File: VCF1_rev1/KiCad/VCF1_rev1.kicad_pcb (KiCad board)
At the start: 4 copper layers, 100 x 95 mm, 190 parts, among them U1 Opamp_Quad, U10 Opamp_Quad, U11 74HC4053, U12 Opamp_Quad, U13 74HC4053, U14 Opamp_Quad, U15 74HC4053, U16 LM13700, U2 74HC4053, U3 CEM3350, U4 Opamp_Quad, U5 LM13700, U6 74HC4053, U7 74HC4053, U8 74HC4053, U9 CEM3350

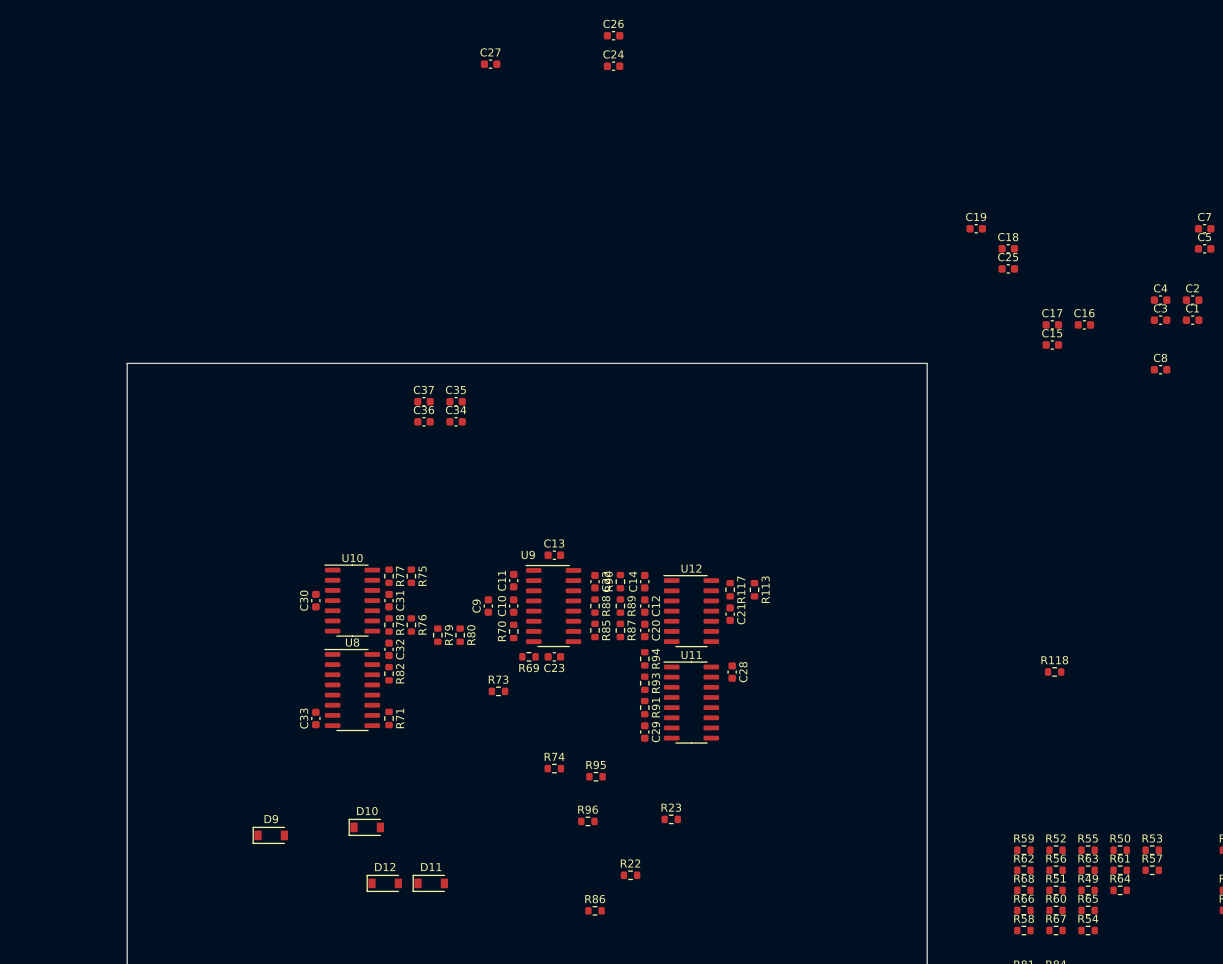
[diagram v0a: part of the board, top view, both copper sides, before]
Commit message: Placed more components on the PCB.
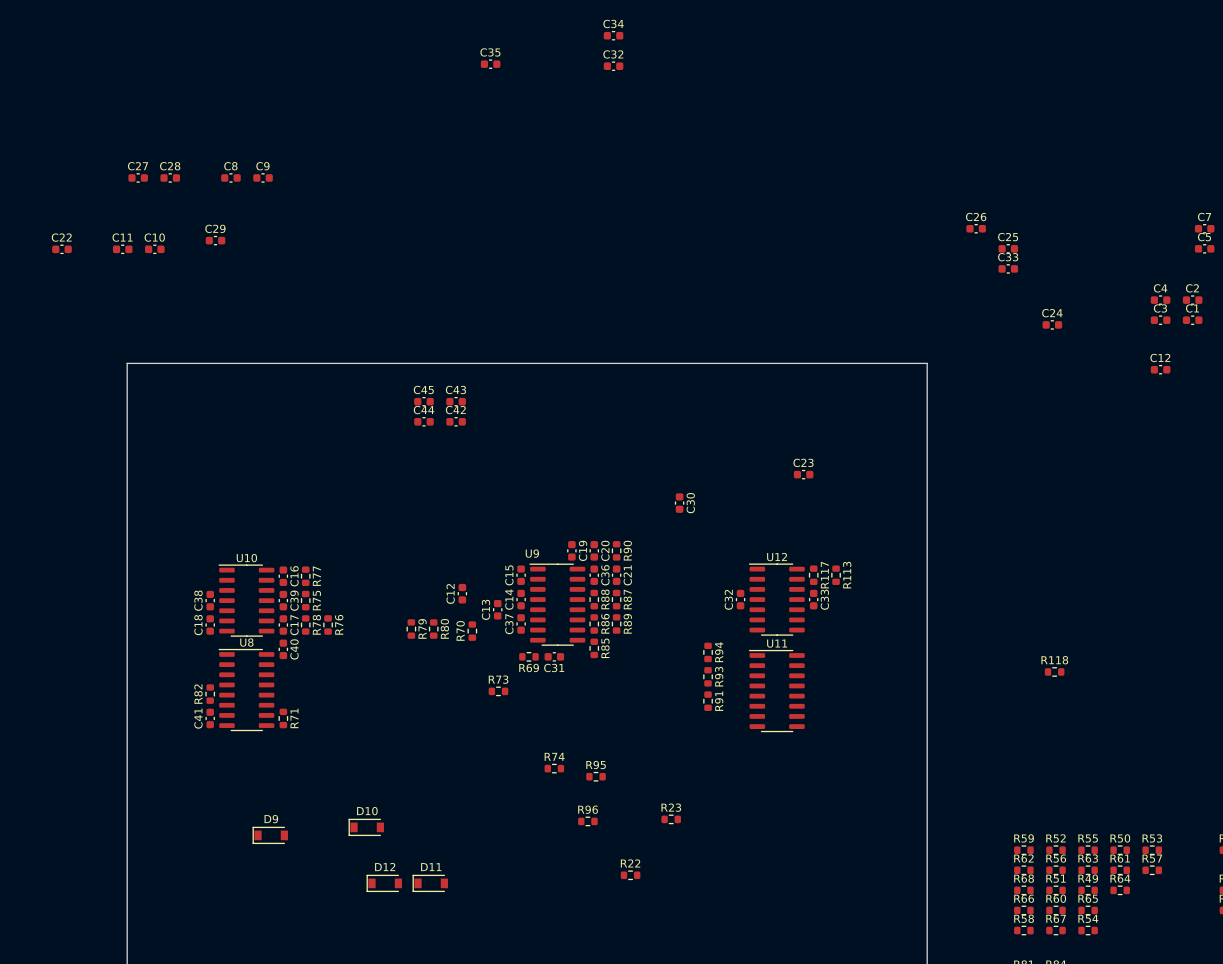
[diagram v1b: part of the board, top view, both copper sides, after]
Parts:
- added C10: C, Capacitor_SMD:C_0603_1608Metric, F.Cu at (116.6, 44.5)
- added C13: 220pF, Capacitor_SMD:C_0603_1608Metric, F.Cu at (159.5, 89.5)
- added C16: C, Capacitor_SMD:C_0603_1608Metric, F.Cu at (132.7, 85.3)
- added C17: C, Capacitor_SMD:C_0603_1608Metric, F.Cu at (132.7, 91.4)
- added C18: C, Capacitor_SMD:C_0603_1608Metric, F.Cu at (123.6, 91.4)
- added C22: C, Capacitor_SMD:C_0603_1608Metric, F.Cu at (105.0, 44.5)
- added C23: C, Capacitor_SMD:C_0603_1608Metric, F.Cu at (197.8, 72.6)
- added C27: C, Capacitor_SMD:C_0603_1608Metric, F.Cu at (114.6, 35.6)
- added C28: C, Capacitor_SMD:C_0603_1608Metric, F.Cu at (118.6, 35.6)
- added C29: C, Capacitor_SMD:C_0603_1608Metric, F.Cu at (124.2, 43.4)
- added C8: C, Capacitor_SMD:C_0603_1608Metric, F.Cu at (126.2, 35.6)
- C11, C9: value 220pF -> C
- moved C21 66.3 mm to (174.4, 85.2), turned to -90 degrees
- moved C11 64.1 mm to (112.6, 44.5), turned to 0 degrees
- moved C20 62.8 mm to (171.6, 82.2), turned to -90 degrees
- moved C9 60.5 mm to (130.2, 35.6), turned to 0 degrees
- moved R86 35.9 mm to (171.6, 91.3), turned to -90 degrees
- moved R82 22.5 mm to (123.6, 100.1), turned to 90 degrees
- moved C36 21.1 mm to (171.6, 85.2)
- moved C37 20.5 mm to (162.4, 91.3), turned to 90 degrees
- moved C14 15.5 mm to (162.4, 88.3), turned to 90 degrees
- moved C30 14.4 mm to (182.2, 76.2)
- moved R75 13.6 mm to (135.5, 88.4)
- moved C38 13.2 mm to (123.6, 88.4)
- moved C39 13.2 mm to (132.7, 88.4)
- moved C40 13.2 mm to (132.7, 94.5)
- moved C41 13.2 mm to (123.6, 103.1)
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- renumbered C8 to C12, C10 to C12, C12 to C14, C13 to C15, C14 to C19, C15 to C20, C16 to C21, C17 to C24, C18 to C25, C19 to C26, C22 to C30, C23 to C31, C20 to C32, C24 to C32, C21 to C33, C25 to C33, C26 to C34, C27 to C35, C28 to C36, C29 to C37, C30 to C38, C31 to C39, C32 to C40, C33 to C41, C34 to C42, C35 to C43, C36 to C44, C37 to C45
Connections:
- C12 pad 1: Net-(C8-Pad1) -> Net-(C12-Pad1)
- C12 pad 2: Net-(C8-Pad2) -> Net-(C12-Pad2)
- C12 pad 1: Net-(C10-Pad1) (its old number) -> Net-(C12-Pad1)
- C12 pad 2: Net-(C10-Pad2) (its old number) -> Net-(C12-Pad2)
- C14 pad 1: Net-(C11-Pad1) -> Net-(C13-Pad1)
- C19 pad 1: Net-(C14-Pad1) -> Net-(C19-Pad1)
- C19 pad 2: Net-(C14-Pad2) -> Net-(C20-Pad2)
- C20 pad 2: Net-(C14-Pad1) -> Net-(C20-Pad2)
- C21 pad 1: Net-(C16-Pad1) -> Net-(D13-Pad1)
- C21 pad 2: Net-(C16-Pad2) (its old number) -> Net-(C21-Pad2)
- C9 pad 1: Net-(C10-Pad1) (its old number) -> Net-(C9-Pad1)
- D13 pad 1: Net-(C16-Pad2) (its old number) -> Net-(D13-Pad1)
- D14 pad 2: Net-(C16-Pad2) (its old number) -> Net-(D13-Pad1)
- R60 pad 1: Net-(R60-Pad1) -> Net-(C11-Pad1)
- R63 pad 1: Net-(R60-Pad1) -> Net-(C11-Pad1)
- R63 pad 2: Net-(R63-Pad2) -> Net-(C11-Pad2)
- R66 pad 1: Net-(R63-Pad2) -> Net-(C11-Pad2)
- R68 pad 1: Net-(C10-Pad1) (its old number) -> Net-(C12-Pad1)
- R82 pad 1: Net-(R82-Pad1) -> GND
- R82 pad 2: GND -> Net-(R82-Pad2)
- R87 pad 2: Net-(R87-Pad2) -> Net-(R88-Pad2)
- R88 pad 2: Net-(R87-Pad1) -> Net-(R88-Pad2)
- R89 pad 1: /VCF_3/VCF3_HP_out -> Net-(R88-Pad2)
- R89 pad 2: Net-(R87-Pad1) -> /VCF_3/VCF3_HP_out
- R90 pad 2: Net-(C16-Pad2) (its old number) -> Net-(D13-Pad1)
- U10 pad 10: Net-(C11-Pad1) -> Net-(C13-Pad1)
- U10 pad 5: Net-(R82-Pad1) -> Net-(R82-Pad2)
- U11 pad 1: Net-(R87-Pad2) -> Net-(R87-Pad1)
- U11 pad 2: Net-(C14-Pad2) -> Net-(C19-Pad1)
- U12 pad 3: Net-(C16-Pad1) -> Net-(C21-Pad2)
- U12 pad 5: Net-(C14-Pad1) -> Net-(C20-Pad2)
- U4 pad 13: Net-(R60-Pad1) -> Net-(C11-Pad1)
- U4 pad 14: unconnected-(U4-Pad14) -> Net-(C11-Pad2)
- U5 pad 9: Net-(C10-Pad1) (its old number) -> Net-(C12-Pad1)
- U7 pad 13: Net-(C10-Pad2) (its old number) -> Net-(C12-Pad2)
- U8 pad 1: unconnected-(U8-Pad1) -> /Controlpanel/VCF2_LP_select
- U8 pad 10: /Controlpanel/VCF2_invert_select -> Net-(R71-Pad1)
- U8 pad 11: Net-(R71-Pad1) -> /Controlpanel/VCF2_HP_select
- U8 pad 12: /MUX/VCF2_send -> /VCF_2/VCF2_LP_BP_out
- U8 pad 13: /Controlpanel/VCF2_LP_select -> /VCF_2/VCF2_HP_out
- U8 pad 14: Net-(C11-Pad2) -> Net-(R81-Pad1)
- U8 pad 15: Net-(R82-Pad1) -> Net-(C13-Pad2)
- U8 pad 2: Net-(R81-Pad1) -> /MUX/VCF2_send
- U8 pad 3: /VCF_2/VCF2_HP_out -> unconnected-(U8-Pad3)
- U8 pad 4: Net-(R81-Pad1) -> Net-(R82-Pad2)
- U8 pad 5: /VCF_2/VCF2_LP_BP_out -> Net-(R81-Pad1)
- U8 pad 9: /Controlpanel/VCF2_HP_select -> /Controlpanel/VCF2_invert_select
- U9 pad 12: Net-(R87-Pad1) -> Net-(R88-Pad2)
- U9 pad 13: Net-(C16-Pad1) -> Net-(C21-Pad2)
- U9 pad 15: Net-(C14-Pad1) -> Net-(C20-Pad2)
- U9 pad 5: Net-(C11-Pad1) -> Net-(C13-Pad1)
